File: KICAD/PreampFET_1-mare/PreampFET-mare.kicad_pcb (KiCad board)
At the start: 2 copper layers, 12 x 10 mm, 18 parts, among them J1 Conn_01x02, J2 Conn_01x04, Q1 JFE2140DSGR, Q2 PMP4501V_115

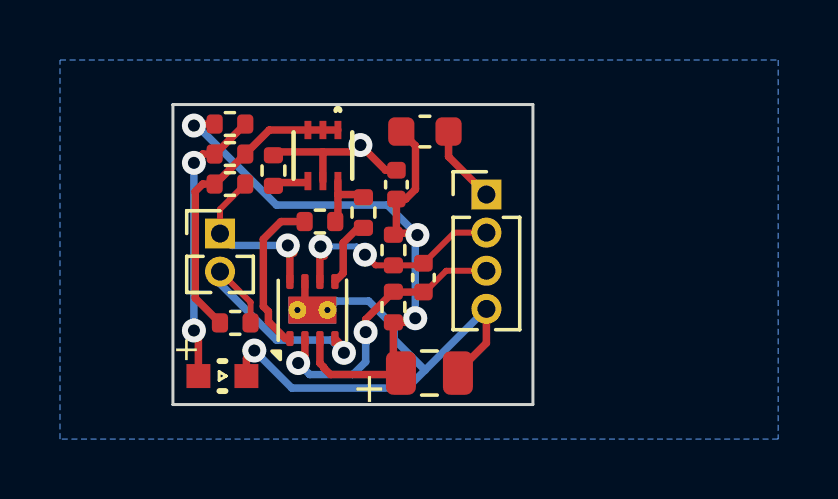
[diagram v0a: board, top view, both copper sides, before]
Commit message: updated for fet-preamp
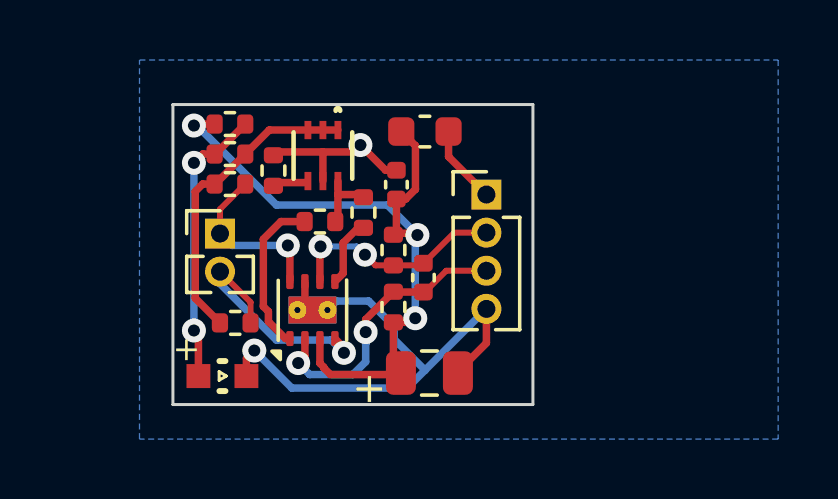
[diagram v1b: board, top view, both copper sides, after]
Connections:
- L1 pad 2: +3V3 -> Vcc
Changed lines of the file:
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@@
 		(pad_to_mask_clearance 0)
 		(allow_soldermask_bridges_in_footprints no)
+		(aux_axis_origin 107.65 80.7)
+		(grid_origin 107.65 80.7)
 		(pcbplotparams
 			(layerselection 0x0021000_7ffffffe)
@@
 	(net 12 "Net-(Q2-Pad4)")
 	(net 13 "Net-(D1-Pad2)")
+	(net 14 "Vcc")
 	(footprint "Connector_PinHeader_1.27mm:PinHeader_1x02_P1.27mm_Vertical"
 		(layer "F.Cu")
@@
 		(tags "inductor")
 		(property "Reference" "L1"
-			(at -2.75 0.275 360)
+			(at -2.75 0.275 0)
 			(layer "F.SilkS")
 			(hide yes)
@@
 		)
 		(property "Footprint" "Inductor_SMD:L_0603_1608Metric"
-			(at 0 0 360)
+			(at 0 0 0)
 			(layer "F.Fab")
 			(hide yes)
@@
 		)
 		(property "Datasheet" ""
-			(at 0 0 360)
+			(at 0 0 0)
 			(layer "F.Fab")
 			(hide yes)
@@
 		)
 		(property "Description" ""
-			(at 0 0 360)
+			(at 0 0 0)
 			(layer "F.Fab")
 			(hide yes)
@@
 		)
 		(fp_text user "${REFERENCE}"
-			(at 0 0 360)
+			(at 0 0 0)
 			(layer "F.Fab")
 			(effects
@@
 			(layers "F.Cu" "F.Paste" "F.Mask")
 			(roundrect_rratio 0.25)
-			(net 3 "+3V3")
+			(net 14 "Vcc")
 			(pinfunction "2")
 			(pintype "passive")
@@
 		(tags "resistor")
 		(property "Reference" "R5"
-			(at 0 -1.17 360)
+			(at 0 -1.17 0)
 			(layer "F.SilkS")
 			(hide yes)
@@
 		)
 		(property "Value" "49.9"
-			(at 0 1.17 360)
+			(at 0 1.17 0)
 			(layer "F.Fab")
 			(effects
@@
 		)
 		(fp_text user "${REFERENCE}"
-			(at 0 0 360)
+			(at 0 0 0)
 			(layer "F.Fab")
 			(effects
@@
 		)
 		(property "Value" "LED 150060VS75000"
-			(at 0 1.2936 360)
+			(at 0 1.2936 0)
 			(layer "F.Fab")
 			(effects
@@
 		)
 		(property "Footprint" "myLibrary:WL-SMCW_0603"
-			(at 0 0 360)
+			(at 0 0 0)
 			(layer "F.Fab")
 			(hide yes)
@@
 		)
 		(property "Datasheet" ""
-			(at 0 0 360)
+			(at 0 0 0)
 			(layer "F.Fab")
 			(hide yes)
@@
 		)
 		(property "Description" "Light emitting diode"
-			(at 0 0 360)
+			(at 0 0 0)
 			(layer "F.Fab")
 			(hide yes)
@@
 		)
 		(fp_text user "+"
-			(at 1.6 0.3 360)
+			(at 1.6 0.3 0)
 			(layer "F.Fab")
 			(effects
@@
 		(tags "capacitor")
 		(property "Reference" "C2"
-			(at 0 -1.68 360)
+			(at 0 -1.68 0)
 			(layer "F.SilkS")
 			(hide yes)
@@
 		)
 		(property "Value" "47u"
-			(at 0 1.68 360)
+			(at 0 1.68 0)
 			(layer "F.Fab")
 			(effects
@@
 		)
 		(fp_text user "${REFERENCE}"
-			(at 0 0 360)
+			(at 0 0 0)
 			(layer "F.Fab")
 			(effects
@@
 		(layer "Dwgs.User")
 		(pts
-			(xy 107.65 70.7) (xy 107.65 80.7)
+			(xy 107.611 70.7) (xy 107.611 80.7)
 		)
-		(height 13.311)
+		(height 2.511)
 		(gr_text "10.0000 mm"
-			(at 92.539 75.7 90)
+			(at 103.3 75.7 90)
 			(layer "Dwgs.User")
 			(effects
@@
 			(xy 107.65 80.7) (xy 119.65 80.7)
 		)
-		(height 7.384)
+		(height 4.45)
 		(gr_text "12.0000 mm"
-			(at 113.65 86.284 0)
+			(at 113.65 83.35 0)
 			(layer "Dwgs.User")
 			(effects
@@
 		(net 1)
 	)
-	(segment
-		(start 114 71.95)
-		(end 113.9 72.05)
-		(width 0.25)
-		(layer "F.Cu")
-		(net 1)
-	)
 	(via
 		(at 110.363 78.9)
@@
 	)
 	(segment
-		(start 112.570455 75.430698)
-		(end 112.570455 75.623081)
-		(width 0.25)
-		(layer "F.Cu")
-		(net 5)
-	)
-	(segment
 		(start 112.55 75.451153)
 		(end 112.55 76.6)
@@
 	)
 	(segment
-		(start 112.570455 75.623081)
-		(end 112.7 75.752626)
-		(width 0.25)
-		(layer "F.Cu")
-		(net 5)
-	)
-	(segment
 		(start 114.403933 76.06)
 		(end 115 76.06)
@@
 	)
 	(segment
-		(start 111.676455 75.592323)
-		(end 111.676455 75.653975)
-		(width 0.25)
-		(layer "F.Cu")
-		(net 7)
-	)
-	(segment
 		(start 110.06 73.35)
 		(end 109.22 74.19)
@@
 	)
 	(segment
-		(start 111.479719 75.395587)
-		(end 111.676455 75.592323)
-		(width 0.25)
-		(layer "F.Cu")
-		(net 7)
-	)
-	(segment
 		(start 111.55 75.465868)
 		(end 111.55 76.6)
@@
 		(polygon
 			(pts
-				(xy 127.8255 81.8515) (xy 103.886 81.8515) (xy 103.886 69.215) (xy 127.8255 69.215)
+				(xy 127.8255 81.8515) (xy 106.536 81.8515) (xy 106.536 69.215) (xy 127.8255 69.215)
 			)
 		)

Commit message: v19-12-24
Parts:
- added C4: 22uF, Capacitor_SMD:C_0603_1608Metric, F.Cu at (114.5, 72.3)
- C1: value 0.1u -> 0.1uF
- C2: value 47u -> 22uF; footprint Capacitor_SMD:C_0805_2012Metric -> Capacitor_SMD:C_0603_1608Metric
- C3: value 150p -> 150pF
- R1, R3: value 10M -> 10M,1%
- R2, R4: value 1k -> 1k,0.1%
- R5, R6: value 49.9 -> 49.9,0.1%
- R7: value 360 -> 360,0.1%
- R8: value 10k -> 10k,1%
- R9: value 3.9k -> 3.9k,1%
- moved C3 2.27 mm to (114.1, 77.7)
- moved L1 1.80 mm to (117.8, 71.6), turned to 180 degrees
- moved C2 1.70 mm to (117.9, 79.7), turned to 180 degrees
- moved R2 1.12 mm to (115.2, 78.5)
- moved R4 1.06 mm to (115.2, 76.6)
- moved C1 0.89 mm to (116.0, 73.7), turned to -90 degrees
- moved R6 0.80 mm to (114.0, 75.1)
- moved Q2 0.25 mm to (112.6, 72.6)
- moved R5 0.05 mm to (112.5, 74.7)
- turned R8 to 180 degrees
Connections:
- C1 pad 1: VC -> Vcc
- C2 pad 1: VC -> Vcc
- J2 pad 1: +3V3 -> Vcc
- L1 pad 1: VC -> Vcc
- L1 pad 2: Vcc -> VC
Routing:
- net Vcc: track 0.00 -> 12.4 mm
- net VC: track 23.7 -> 20.4 mm
- net +3V3: track 2.62 -> 0.00 mm
- net GND: track 24.1 -> 26.1 mm
- net Net-(Q1-Pad5): track 2.29 -> 1.41 mm
- net /B+: track 7.42 -> 8.25 mm
